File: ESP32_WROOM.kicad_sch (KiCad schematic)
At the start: 17 parts, among them J5 UART LED Debug Switch, J7 Programming Socket, Q1 NPN, Q2 NPN, SW1 EN, SW2 EN, U11 NTS0104GU12_115, U6 ESP32-WROOM-32E

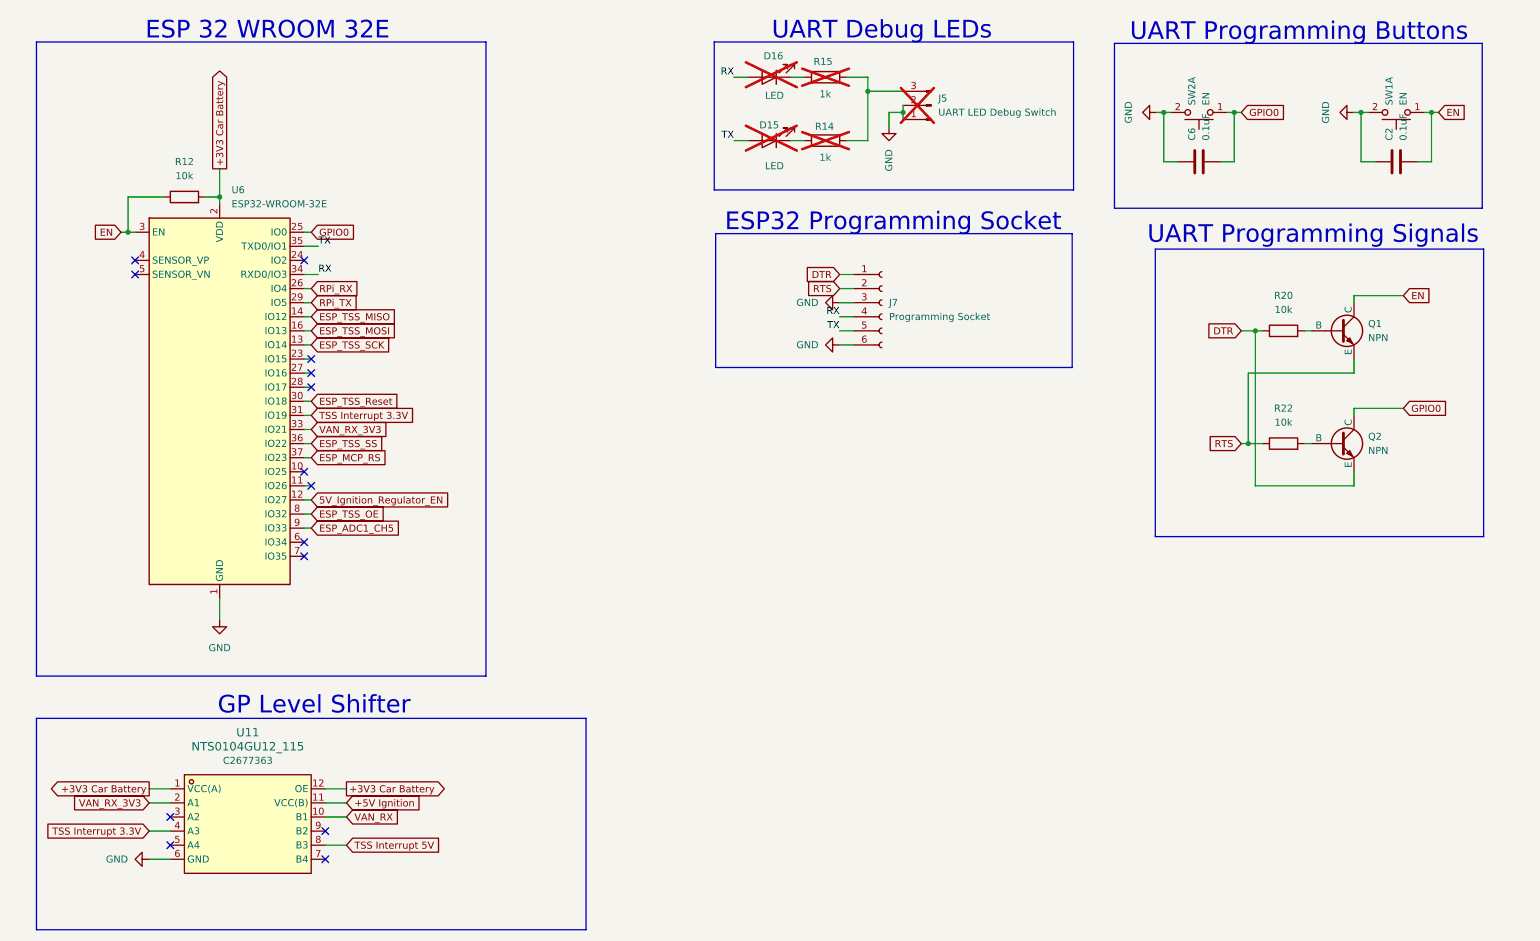
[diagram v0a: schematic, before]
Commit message: implemented the changes from 'Board defects'
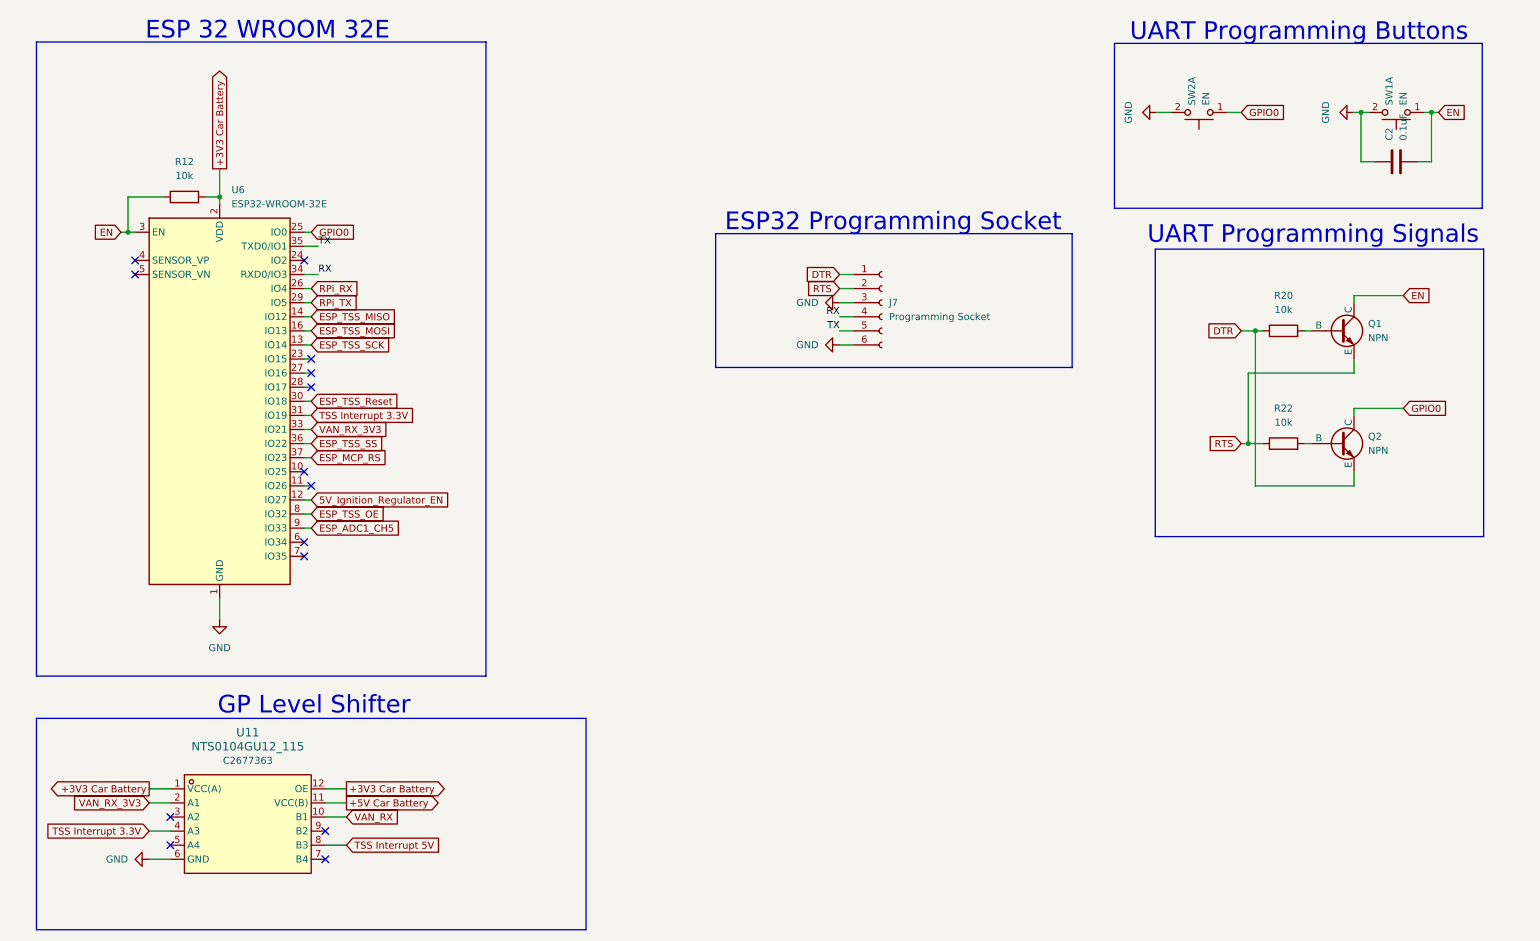
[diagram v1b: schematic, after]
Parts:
- removed C6: 0.1uF, Capacitor_SMD:C_0805_2012Metric, symbol Device:C
- removed D15, D16: LED, LED_SMD:LED_0402_1005Metric, symbol Device:LED
- removed J5: UART LED Debug Switch, Connector_PinHeader_2.54mm:PinHeader_1x03_P2.54mm_Vertical, symbol Connector:Conn_01x03_Pin
- removed R14, R15: 1k, Resistor_SMD:R_0805_2012Metric, symbol Device:R
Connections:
- net +5V Ignition renamed +5V Car Battery
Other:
- note removed: "UART Debug LEDs"

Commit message: 2 layer PCB
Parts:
- U6: footprint RF_Module:ESP32-WROOM-32D -> intoftainment:esp32_altered
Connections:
- net ESP_TSS_Reset is gone; now on net ESP_TSS_OE: U6.30 (IO18)
- net ESP_TSS_OE: no longer U6.8 (IO32)
- net ESP_TSS_SCK: now also U11.4 (A3)
- net TSS Interrupt 3.3V: no longer U11.4 (A3)
- net ESP_MCP_RS: no longer names the net of U6.37 (IO23)
- net TSS Interrupt 5V renamed TSS_CLK
- no-connect marks 14 -> 16

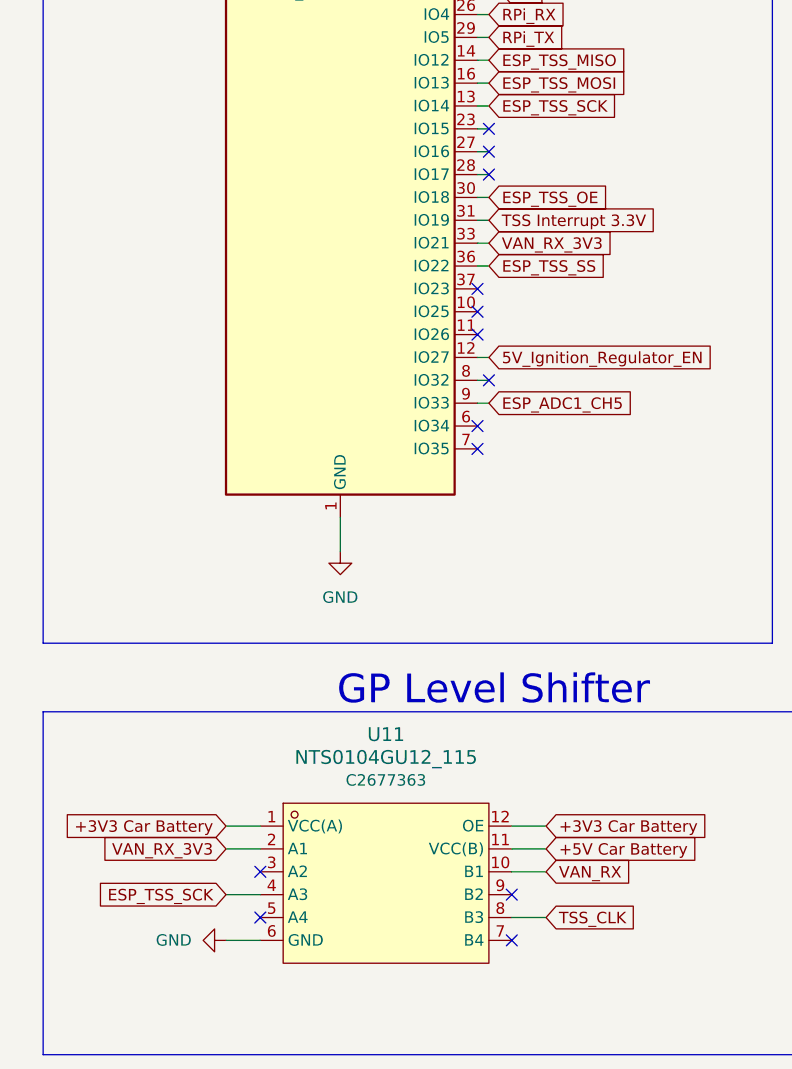
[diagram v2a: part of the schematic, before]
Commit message: changed the CAN transceiever; fixed the transiever typo
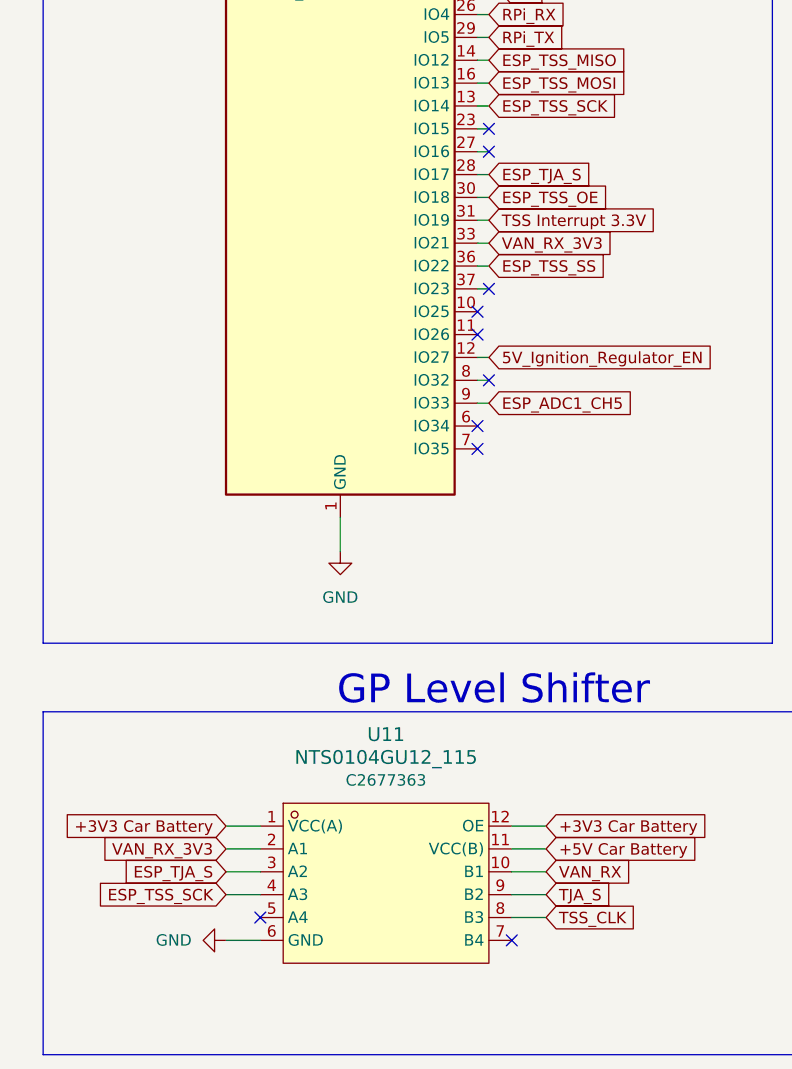
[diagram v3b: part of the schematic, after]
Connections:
- net ESP_TJA_S: now reaches U6.28 (IO17)
- net ESP_TJA_S: now also U11.3 (A2)
- net TJA_S: now reaches U11.9 (B2)
- no-connect marks 16 -> 13
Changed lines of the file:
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@@
-	)
-	(no_connect
-		(at 67.31 80.01)
 	)
 	(no_connect
@@
 	)
 	(no_connect
-		(at 67.31 74.93)
+		(at 67.31 92.71)
 	)
 	(no_connect
@@
 	)
 	(no_connect
-		(at 69.85 160.02)
+		(at 66.04 57.15)
 	)
 	(no_connect
-		(at 66.04 92.71)
-	)
-	(no_connect
-		(at 66.04 57.15)
+		(at 67.31 74.93)
 	)
 	(no_connect
@@
 		(at 67.31 77.47)
 	)
-	(no_connect
-		(at 41.91 157.48)
-	)
 	(wire
 		(pts
@@
 	(wire
 		(pts
+			(xy 66.04 92.71) (xy 67.31 92.71)
+		)
+		(stroke
+			(width 0)
+			(type default)
+		)
+	)
+	(wire
+		(pts
 			(xy 255.27 30.48) (xy 256.54 30.48)
 		)
@@
 	(wire
 		(pts
+			(xy 38.1 157.48) (xy 41.91 157.48)
+		)
+		(stroke
+			(width 0)
+			(type default)
+		)
+	)
+	(wire
+		(pts
 			(xy 34.29 45.72) (xy 34.29 52.07)
 		)
@@
 	(wire
 		(pts
+			(xy 69.85 160.02) (xy 73.66 160.02)
+		)
+		(stroke
+			(width 0)
+			(type default)
+		)
+	)
+	(wire
+		(pts
 			(xy 66.04 80.01) (xy 67.31 80.01)
 		)
@@
 		)
 	)
+	(global_label "ESP_TJA_S"
+		(shape input)
+		(at 67.31 80.01 0)
+		(fields_autoplaced yes)
+		(effects
+			(font
+				(size 1.27 1.27)
+			)
+			(justify left)
+		)
+		(property "Intersheetrefs" "${INTERSHEET_REFS}"
+			(at 80.0922 80.01 0)
+			(effects
+				(font
+					(size 1.27 1.27)
+				)
+				(justify left)
+				(hide yes)
+			)
+		)
+	)
 	(global_label "GPIO0"
 		(shape input)
@@
 		)
 	)
+	(global_label "ESP_TJA_S"
+		(shape input)
+		(at 38.1 157.48 180)
+		(fields_autoplaced yes)
+		(effects
+			(font
+				(size 1.27 1.27)
+			)
+			(justify right)
+		)
+		(property "Intersheetrefs" "${INTERSHEET_REFS}"
+			(at 25.3178 157.48 0)
+			(effects
+				(font
+					(size 1.27 1.27)
+				)
+				(justify right)
+				(hide yes)
+			)
+		)
+	)
 	(global_label "RPi_RX"
 		(shape input)
@@
 			(effects
 				(font
+					(size 1.27 1.27)
+				)
+				(justify left)
+				(hide yes)
+			)
+		)
+	)
+	(global_label "TJA_S"
+		(shape input)
+		(at 73.66 160.02 0)
+		(fields_autoplaced yes)
+		(effects
+			(font
+				(size 1.27 1.27)
+			)
+			(justify left)
+		)
+		(property "Intersheetrefs" "${INTERSHEET_REFS}"
+			(at 81.8461 160.02 0)
+			(effects
+				(font

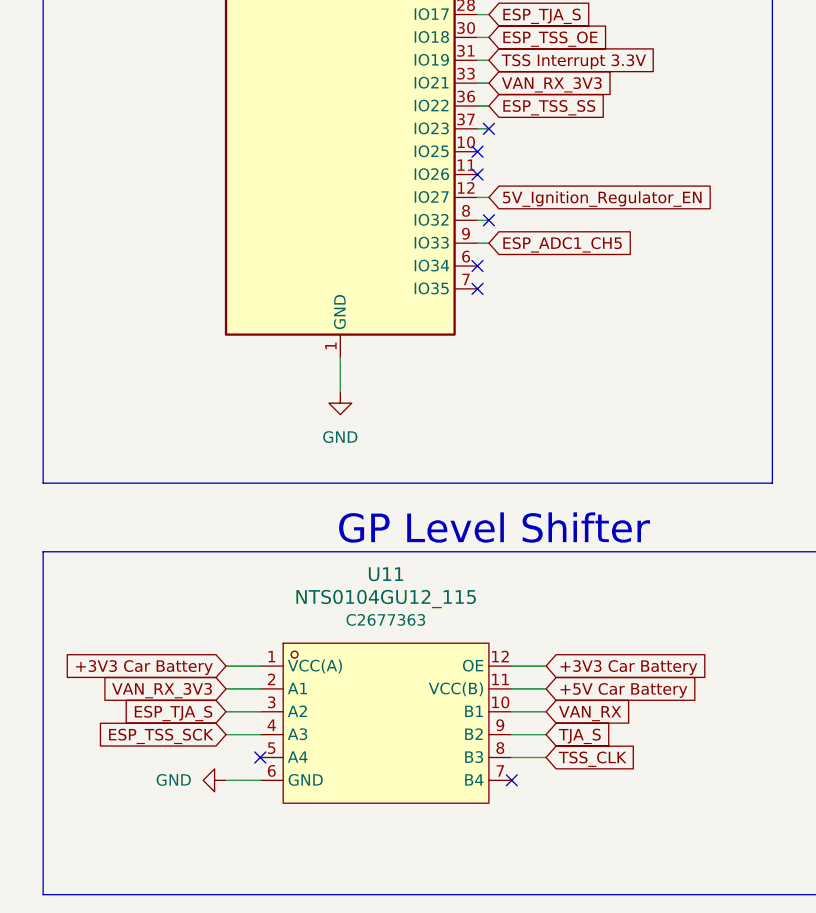
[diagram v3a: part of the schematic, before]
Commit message: added direct VAN_TX to ESP connection
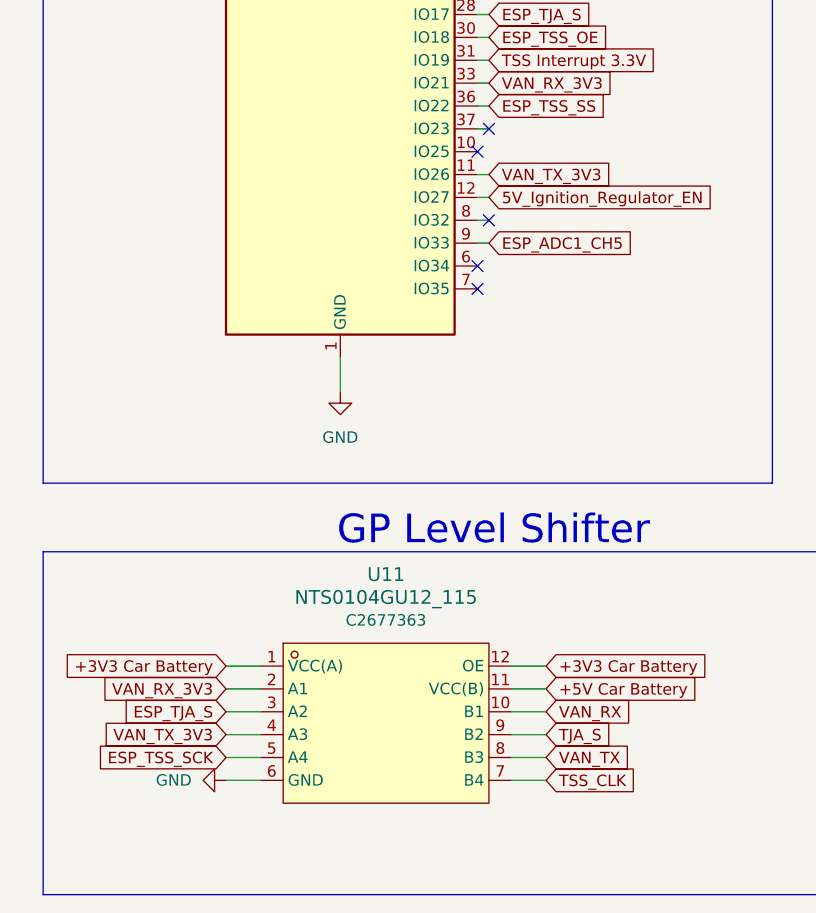
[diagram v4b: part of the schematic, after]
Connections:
- net ESP_TSS_SCK: now also U11.5 (A4); no longer U11.4 (A3)
- net TSS_CLK: now also U11.7 (B4); no longer U11.8 (B3)
- net VAN_TX_3V3: now reaches U6.11 (IO26)
- net VAN_TX_3V3: now also U11.4 (A3)
- new net VAN_TX: U11.8 (B3)
- no-connect marks 13 -> 10
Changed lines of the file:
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@@
-	)
-	(no_connect
-		(at 41.91 162.56)
 	)
 	(no_connect
@@
 	)
 	(no_connect
-		(at 69.85 165.1)
-	)
-	(no_connect
-		(at 66.04 97.79)
-	)
-	(no_connect
 		(at 66.04 95.25)
 	)
@@
 	(wire
 		(pts
+			(xy 38.1 162.56) (xy 41.91 162.56)
+		)
+		(stroke
+			(width 0)
+			(type default)
+		)
+	)
+	(wire
+		(pts
 			(xy 270.51 30.48) (xy 269.24 30.48)
 		)
@@
 	(wire
 		(pts
+			(xy 66.04 97.79) (xy 67.31 97.79)
+		)
+		(stroke
+			(width 0)
+			(type default)
+		)
+	)
+	(wire
+		(pts
 			(xy 66.04 105.41) (xy 67.31 105.41)
 		)
@@
 	(wire
 		(pts
+			(xy 69.85 165.1) (xy 73.66 165.1)
+		)
+		(stroke
+			(width 0)
+			(type default)
+		)
+	)
+	(wire
+		(pts
 			(xy 255.27 83.82) (xy 264.16 83.82)
 		)
@@
 		)
 	)
+	(global_label "VAN_TX"
+		(shape input)
+		(at 73.66 162.56 0)
+		(fields_autoplaced yes)
+		(effects
+			(font
+				(size 1.27 1.27)
+			)
+			(justify left)
+		)
+		(property "Intersheetrefs" "${INTERSHEET_REFS}"
+			(at 83.2976 162.56 0)
+			(effects
+				(font
+					(size 1.27 1.27)
+				)
+				(justify left)
+				(hide yes)
+			)
+		)
+	)
 	(global_label "GPIO0"
 		(shape input)
@@
 		)
 	)
+	(global_label "ESP_TSS_SCK"
+		(shape input)
+		(at 38.1 162.56 180)
+		(fields_autoplaced yes)
+		(effects
+			(font
+				(size 1.27 1.27)
+			)
+			(justify right)
+		)
+		(property "Intersheetrefs" "${INTERSHEET_REFS}"
+			(at 22.3199 162.56 0)
+			(effects
+				(font
+					(size 1.27 1.27)
+				)
+				(justify right)
+				(hide yes)
+			)
+		)
+	)
+	(global_label "VAN_TX_3V3"
+		(shape input)
+		(at 38.1 160.02 180)
+		(fields_autoplaced yes)
+		(effects
+			(font
+				(size 1.27 1.27)
+			)
+			(justify right)
+		)
+		(property "Intersheetrefs" "${INTERSHEET_REFS}"
+			(at 23.9872 160.02 0)
+			(effects
+				(font
+					(size 1.27 1.27)
+				)
+				(justify right)
+				(hide yes)
+			)
+		)
+	)
 	(global_label "+3V3 Car Battery"
 		(shape input)
@@
 		)
 	)
+	(global_label "VAN_TX_3V3"
+		(shape input)
+		(at 67.31 97.79 0)
+		(fields_autoplaced yes)
+		(effects
+			(font
+				(size 1.27 1.27)
+			)
+			(justify left)
+		)
+		(property "Intersheetrefs" "${INTERSHEET_REFS}"
+			(at 81.4228 97.79 0)
+			(effects
+				(font
+					(size 1.27 1.27)
+				)
+				(justify left)
+				(hide yes)
+			)
+		)
+	)
 	(global_label "EN"
 		(shape input)
@@
 		)
 	)
+	(global_label "TSS_CLK"
+		(shape input)
+		(at 73.66 165.1 0)
+		(fields_autoplaced yes)
+		(effects
+			(font
+				(size 1.27 1.27)
+			)
+			(justify left)
+		)
+		(property "Intersheetrefs" "${INTERSHEET_REFS}"
+			(at 84.5675 165.1 0)
+			(effects
+				(font
+					(size 1.27 1.27)
+				)
+				(justify left)
+				(hide yes)
+			)
+		)
+	)
 	(global_label "TX"
 		(shape input)
@@
 			(effects
 				(font
-					(size 1.27 1.27)
-				)
-				(justify left)
-				(hide yes)
-			)
-		)
-	)
-	(global_label "ESP_TSS_SCK"
-		(shape input)
-		(at 38.1 160.02 180)
-		(fields_autoplaced yes)
-		(effects
-			(font
-				(size 1.27 1.27)
-			)
-			(justify right)
-		)
-		(property "Intersheetrefs" "${INTERSHEET_REFS}"
-			(at 22.3199 160.02 0)
-			(effects
-				(font
-					(size 1.27 1.27)
-				)
-				(justify right)
-				(hide yes)
-			)
-		)
-	)
-	(global_label "TSS_CLK"
-		(shape input)
-		(at 73.66 162.56 0)
-		(fields_autoplaced yes)
-		(effects
-			(font
-				(size 1.27 1.27)
-			)
-			(justify left)
-		)
-		(property "Intersheetrefs" "${INTERSHEET_REFS}"
-			(at 84.5675 162.56 0)
-			(effects
-				(font
